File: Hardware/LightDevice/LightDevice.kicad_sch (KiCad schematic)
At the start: 9 parts, among them J1 LED Strip 0, J2 LED Strip 1, J3 LED Strip 2, J4 LED Strip 3, J5 LED Strip 4, J6 LED Strip 5, J7 LED Strip 6, J8 LED Strip 7

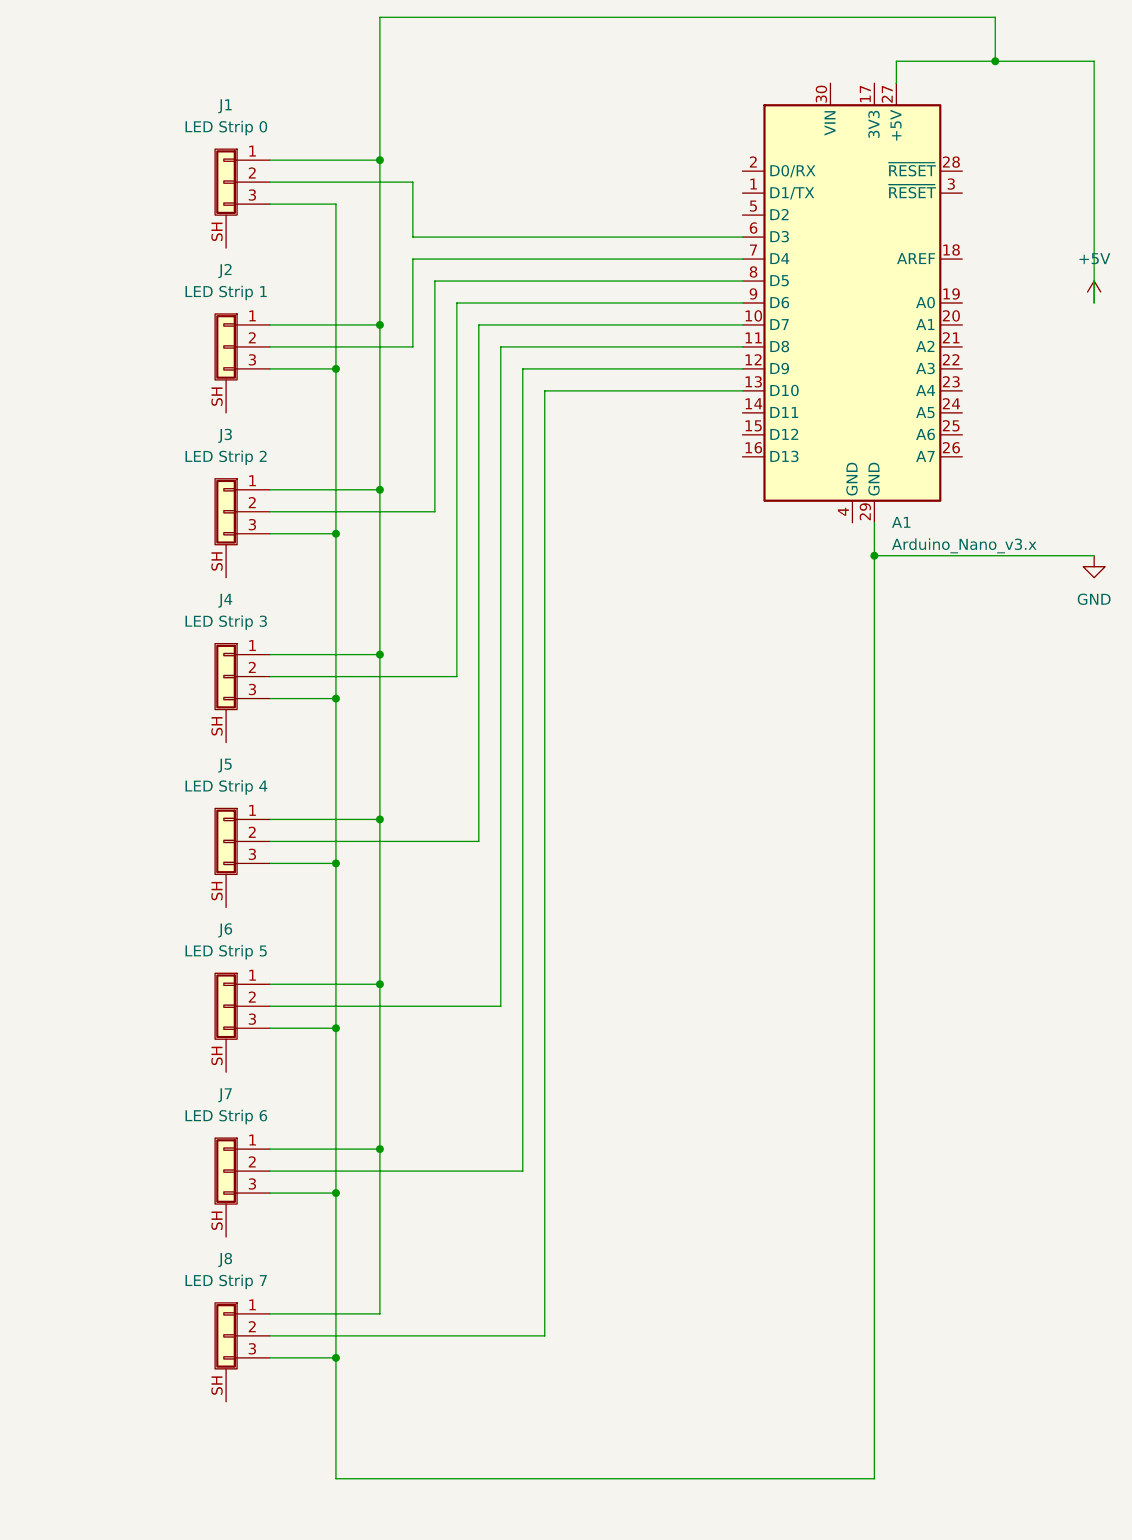
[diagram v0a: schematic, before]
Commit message: More support for multistrip
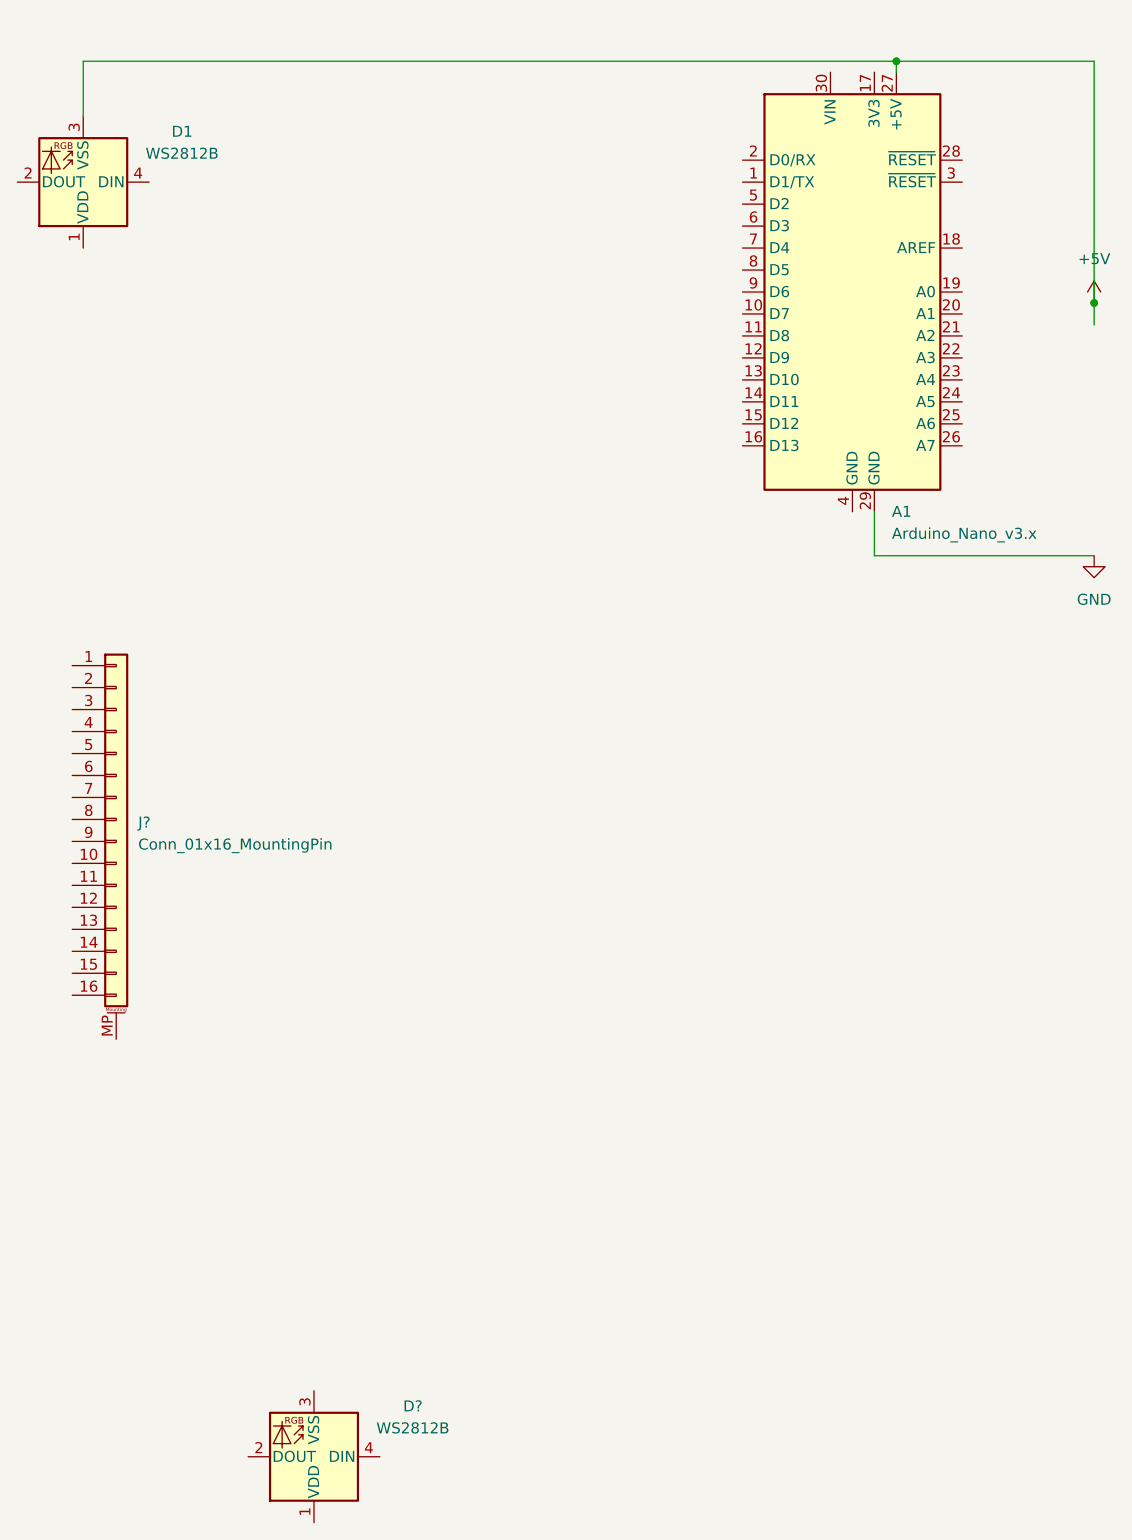
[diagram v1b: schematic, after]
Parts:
- removed J1: LED Strip 0, symbol Connector_Generic_Shielded:Conn_01x03_Shielded
- removed J2: LED Strip 1, symbol Connector_Generic_Shielded:Conn_01x03_Shielded
- removed J3: LED Strip 2, symbol Connector_Generic_Shielded:Conn_01x03_Shielded
- removed J4: LED Strip 3, symbol Connector_Generic_Shielded:Conn_01x03_Shielded
- removed J5: LED Strip 4, symbol Connector_Generic_Shielded:Conn_01x03_Shielded
- removed J6: LED Strip 5, symbol Connector_Generic_Shielded:Conn_01x03_Shielded
- removed J7: LED Strip 6, symbol Connector_Generic_Shielded:Conn_01x03_Shielded
- removed J8: LED Strip 7, symbol Connector_Generic_Shielded:Conn_01x03_Shielded
- added D1, D?: WS2812B, LED_SMD:LED_WS2812B_PLCC4_5.0x5.0mm_P3.2mm, symbol LED:WS2812B
- added J?: Conn_01x16_MountingPin, symbol Connector_Generic_MountingPin:Conn_01x16_MountingPin
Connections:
- net +5V: now also D1.3 (VSS)
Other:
- moved on the sheet: A1

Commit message: Schematic and history images
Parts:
- removed J?: Conn_01x16_MountingPin, symbol Connector_Generic_MountingPin:Conn_01x16_MountingPin
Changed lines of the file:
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@@
     (pin "1")
-  )
-  (symbol (lib_id "Connector_Generic_MountingPin:Conn_01x16_MountingPin") (at 82.55 114.3 0) (unit 1)
-    (in_bom yes) (on_board yes) (fields_autoplaced)
-    (property "Reference" "J?" (id 0) (at 85.09 114.6555 0)
-      (effects (font (size 1.27 1.27)) (justify left))
-    )
-    (property "Value" "Conn_01x16_MountingPin" (id 1) (at 85.09 117.1955 0)
-      (effects (font (size 1.27 1.27)) (justify left))
-    )
-    (property "Footprint" "" (id 2) (at 82.55 114.3 0)
-      (effects (font (size 1.27 1.27)) hide)
-    )
-    (property "Datasheet" "~" (id 3) (at 82.55 114.3 0)
-      (effects (font (size 1.27 1.27)) hide)
-    )
-    (pin "1")
-    (pin "10")
-    (pin "11")
-    (pin "12")
-    (pin "13")
-    (pin "14")
-    (pin "15")
-    (pin "16")
-    (pin "2")
-    (pin "3")
-    (pin "4")
-    (pin "5")
-    (pin "6")
-    (pin "7")
-    (pin "8")
-    (pin "9")
-    (pin "MP")
   )
   (sheet_instances
@@
       (reference "D?") (unit 1) (value "WS2812B") (footprint "LED_SMD:LED_WS2812B_PLCC4_5.0x5.0mm_P3.2mm")
     )
-    (path "/ebd2ad5d-65cf-4f93-b455-c3eb8068258f"
-      (reference "J?") (unit 1) (value "Conn_01x16_MountingPin") (footprint "")
-    )
   )
